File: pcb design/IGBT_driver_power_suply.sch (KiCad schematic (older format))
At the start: 53 parts, among them Q15 CSD19533Q5A, Q16 CSD19533Q5A, T1 TRANS-3-1CT, U2 LM5030

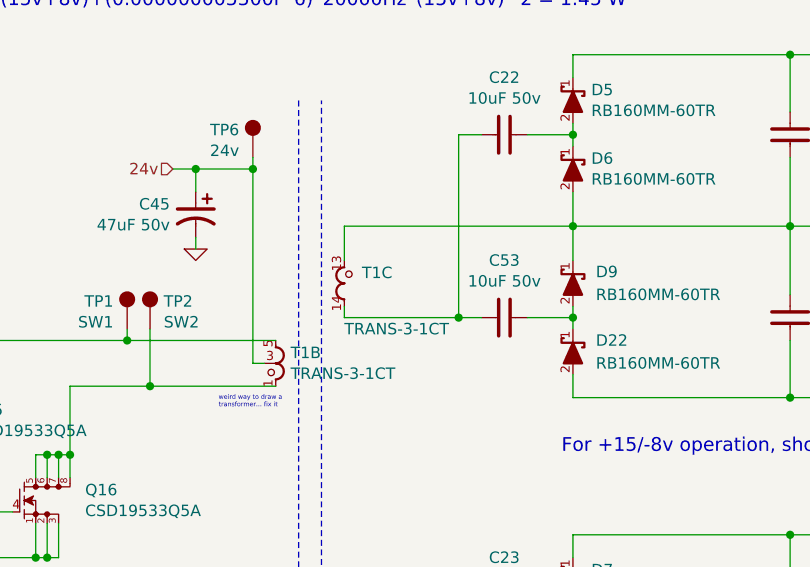
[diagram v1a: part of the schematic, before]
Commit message: Added current sensor connector. Layout is now symmetrical
Signed-off-by: Marcos Chaparro <mchaparro@paltatech.com>
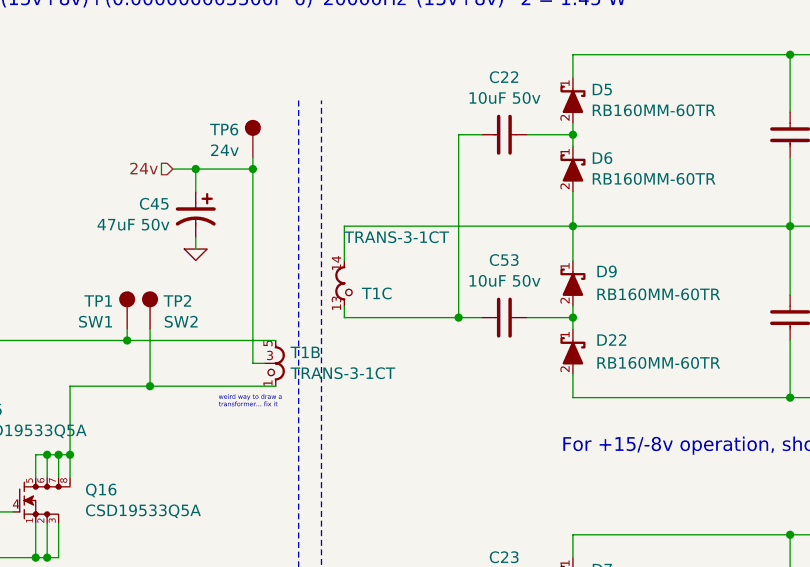
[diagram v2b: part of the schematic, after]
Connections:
- net GND_TOP: now also T1.14; no longer T1.13
- net at C22.2, C53.2: now also T1.13; no longer T1.14
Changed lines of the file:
@@
 $EndComp
 $Comp
-L GND #PWR08
+L GND #PWR21
 U 1 1 582356E3
 P 2950 3500
-F 0 "#PWR08" H 2950 3500 30  0001 C CNN
+F 0 "#PWR21" H 2950 3500 30  0001 C CNN
 F 1 "GND" H 2950 3430 30  0001 C CNN
 F 2 "" H 2950 3500 60  0000 C CNN
@@
 $EndComp
 $Comp
-L GND #PWR09
+L GND #PWR22
 U 1 1 58235BA0
 P 3200 3500
-F 0 "#PWR09" H 3200 3500 30  0001 C CNN
+F 0 "#PWR22" H 3200 3500 30  0001 C CNN
 F 1 "GND" H 3200 3430 30  0001 C CNN
 F 2 "" H 3200 3500 60  0000 C CNN
@@
 $EndComp
 $Comp
-L GND #PWR010
+L GND #PWR19
 U 1 1 58235E8A
 P 2000 4650
-F 0 "#PWR010" H 2000 4650 30  0001 C CNN
+F 0 "#PWR19" H 2000 4650 30  0001 C CNN
 F 1 "GND" H 2000 4580 30  0001 C CNN
 F 2 "" H 2000 4650 60  0000 C CNN
@@
 $EndComp
 $Comp
-L GND #PWR011
+L GND #PWR20
 U 1 1 58235EBE
 P 2250 4450
-F 0 "#PWR011" H 2250 4450 30  0001 C CNN
+F 0 "#PWR20" H 2250 4450 30  0001 C CNN
 F 1 "GND" H 2250 4380 30  0001 C CNN
 F 2 "" H 2250 4450 60  0000 C CNN
@@
 $EndComp
 $Comp
-L GND #PWR012
+L GND #PWR18
 U 1 1 582361AD
 P 1600 4650
-F 0 "#PWR012" H 1600 4650 30  0001 C CNN
+F 0 "#PWR18" H 1600 4650 30  0001 C CNN
 F 1 "GND" H 1600 4580 30  0001 C CNN
 F 2 "" H 1600 4650 60  0000 C CNN
@@
 $EndComp
 $Comp
-L GND #PWR013
+L GND #PWR25
 U 1 1 58236F6A
 P 3900 5150
-F 0 "#PWR013" H 3900 5150 30  0001 C CNN
+F 0 "#PWR25" H 3900 5150 30  0001 C CNN
 F 1 "GND" H 3900 5080 30  0001 C CNN
 F 2 "" H 3900 5150 60  0000 C CNN
@@
 $EndComp
 $Comp
-L GND #PWR014
+L GND #PWR26
 U 1 1 582370C3
 P 4450 5150
-F 0 "#PWR014" H 4450 5150 30  0001 C CNN
+F 0 "#PWR26" H 4450 5150 30  0001 C CNN
 F 1 "GND" H 4450 5080 30  0001 C CNN
 F 2 "" H 4450 5150 60  0000 C CNN
@@
 $EndComp
 $Comp
-L GND #PWR015
+L GND #PWR17
 U 1 1 582389B6
 P 1200 4650
-F 0 "#PWR015" H 1200 4650 30  0001 C CNN
+F 0 "#PWR17" H 1200 4650 30  0001 C CNN
 F 1 "GND" H 1200 4580 30  0001 C CNN
 F 2 "" H 1200 4650 60  0000 C CNN
@@
 $EndComp
 $Comp
-L GND #PWR016
+L GND #PWR24
 U 1 1 5823969B
 P 3550 4500
-F 0 "#PWR016" H 3550 4500 30  0001 C CNN
+F 0 "#PWR24" H 3550 4500 30  0001 C CNN
 F 1 "GND" H 3550 4430 30  0001 C CNN
 F 2 "" H 3550 4500 60  0000 C CNN
@@
 $EndComp
 $Comp
-L GND #PWR017
+L GND #PWR23
 U 1 1 582397EE
 P 3350 5150
-F 0 "#PWR017" H 3350 5150 30  0001 C CNN
+F 0 "#PWR23" H 3350 5150 30  0001 C CNN
 F 1 "GND" H 3350 5080 30  0001 C CNN
 F 2 "" H 3350 5150 60  0000 C CNN
@@
 Connection ~ 5650 2800
 $Comp
-L GND #PWR018
+L GND #PWR27
 U 1 1 5827420A
 P 5650 3150
-F 0 "#PWR018" H 5650 3150 30  0001 C CNN
+F 0 "#PWR27" H 5650 3150 30  0001 C CNN
 F 1 "GND" H 5650 3080 30  0001 C CNN
 F 2 "" H 5650 3150 60  0000 C CNN
@@
 $Bitmap
 Pos 6200 7150
-Scale 1.000000
+Scale 1,000000
 Data
 89 50 4E 47 0D 0A 1A 0A 00 00 00 0D 49 48 44 52 00 00 01 8A 00 00 01 15 08 02 00 00 00 71 2C 35
@@
 F 4 "750342312" H 6300 3300 60  0001 C CNN "mfg#"
 	3    6300 3300
-	1    0    0    -1
+	1    0    0    1
 $EndComp
 Wire Wire Line
@@
 $Bitmap
 Pos 1900 6750
-Scale 1.000000
+Scale 1,000000
 Data
 89 50 4E 47 0D 0A 1A 0A 00 00 00 0D 49 48 44 52 00 00 03 4B 00 00 02 57 08 02 00 00 00 CD 45 58

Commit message: Add gate driver load to enable 2 step turnoff in buffered configuration. Updated layout.
Signed-off-by: Marcos Chaparro <mchaparro@paltatech.com>
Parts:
- C17, C18, C20, C21, C50: symbol C-0603 -> pasv-cap:C-0603
- C19: symbol C-0805 -> pasv-cap:C-0805
- C22, C23, C53, C54: symbol C-1206 -> pasv-cap:C-1206; MPN (none) -> CL31A106KBHNNNE
- C24, C25, C26, C27: symbol C-1206 -> pasv-cap:C-1206; MPN (none) -> CL31A106KBHNNNE; mfg# CL31B106KBHNNNE -> CL31A106KBHNNNE
- C28, C29, C30, C31: symbol C-0805 -> pasv-cap:C-0805; MPN (none) -> 08055C104JAT2A
- C32, C33, C34, C35, C45: symbol C-ALUM-6.3mm -> pasv-cap:C-ALUM-6.3mm; MPN (none) -> EEE-FK1H470XP
- D10, D22, D23, D5, D6, D7, D8, D9: symbol SCHOTTKY -> _semi:SCHOTTKY; MPN (none) -> RB160MM-60TR
- DZ2: value 12v zener -> MM3Z12VB; symbol ZENER -> _semi:ZENER; MPN (none) -> MM3Z12VB
- Q15, Q16: symbol CSD19534Q5A -> semi-trans-TI:CSD19534Q5A; MPN (none) -> CSD19533Q5A
- R34, R35, R36, R37, R38, R39, R40: symbol R-0603 -> pasv-res:R-0603
- R41: symbol R-1206 -> pasv-res:R-1206
- T1: symbol TRANS-wurth_750342312 -> paltatech:TRANS-wurth_750342312; MPN (none) -> 750342312
- TP1, TP10, TP11, TP12, TP2, TP6, TP7, TP8, TP9: symbol TESTPOINT -> pcb:TESTPOINT; version (none) -> none
- U2: symbol LM5030 -> paltatech:LM5030; MPN (none) -> LM5030MM/NOPB
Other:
- note added: "Ensure <30pF transformer capacitance\nLess in case of SiC drives.where 5pF\nwill inject 250mA at 50V/ns (dV/dt) in the\ncontrol side.\nAdding mounting point for grounding these\nswitching currents to the chassis so they\ndon't travel across control wiring."
